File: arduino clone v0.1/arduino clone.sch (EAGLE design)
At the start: 19 parts, among them J202 FTDI Breakout Header, U101 ATMEGA328P_TQFP, U201 CH340G

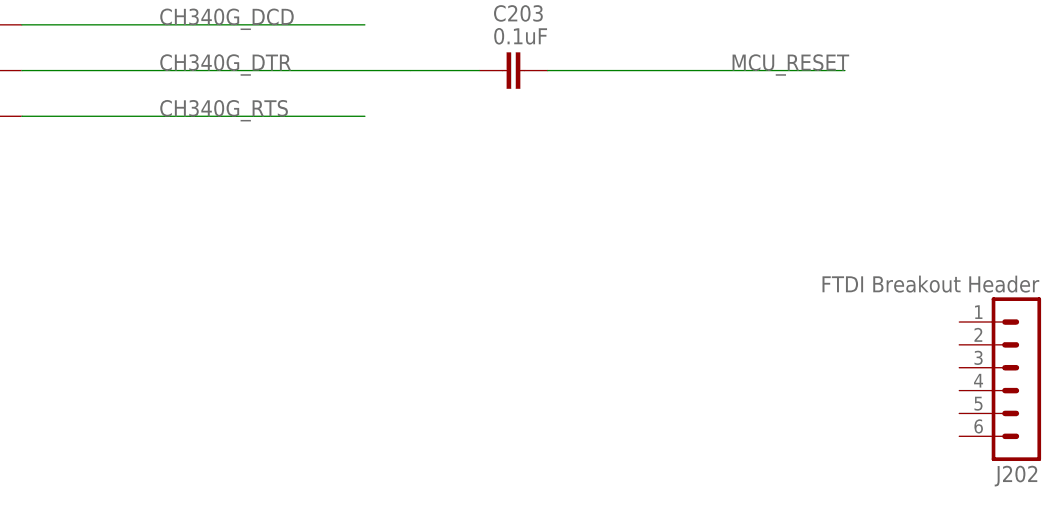
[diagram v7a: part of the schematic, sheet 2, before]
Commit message: add nets from FDTI headers to power and CTS
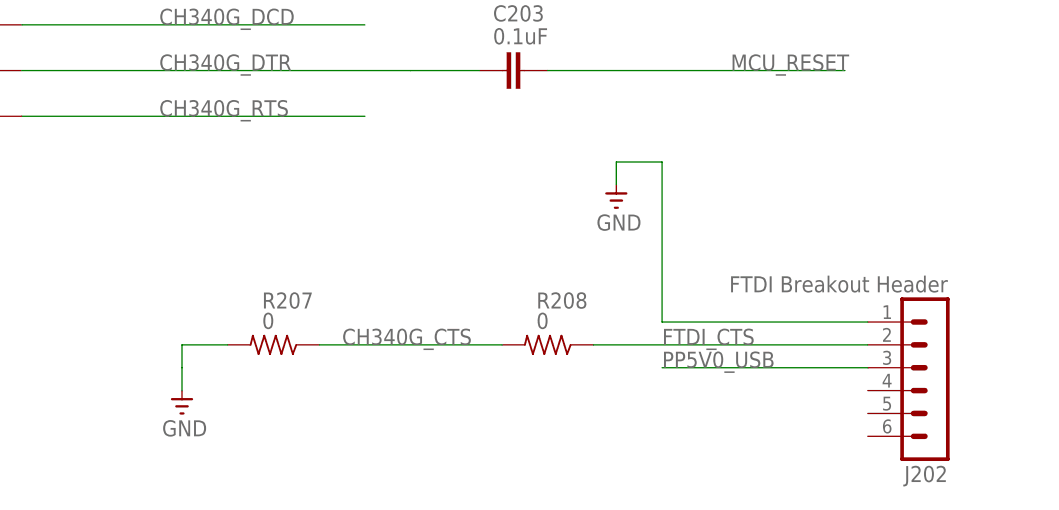
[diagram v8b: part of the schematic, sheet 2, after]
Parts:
- added R207, R208: 0, adafruit:R-US_R0805
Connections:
- new net FTDI_CTS: J202.2, R208.1
- net CH340G_CTS: now also R207.1, R208.2
- net GND: now also J202.1, R207.2
- net PP5V0_USB: now also J202.3
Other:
- moved on the sheet: J202
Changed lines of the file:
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@@
 <part name="C203" library="rcl" library_urn="urn:adsk.eagle:library:334" deviceset="C-EU" device="C0805" package3d_urn="urn:adsk.eagle:package:23617/2" value="0.1uF"/>
 <part name="J202" library="con-lstb" library_urn="urn:adsk.eagle:library:162" deviceset="MA06-1" device="" package3d_urn="urn:adsk.eagle:package:8340/1" value="FTDI Breakout Header"/>
+<part name="GND12" library="supply" deviceset="GND" device=""/>
+<part name="R208" library="adafruit" deviceset="R-US_" device="R0805" value="0"/>
+<part name="R207" library="adafruit" deviceset="R-US_" device="R0805" value="0"/>
+<part name="GND13" library="supply" deviceset="GND" device=""/>
 </parts>
 <sheets>
@@
 <attribute name="VALUE" x="293.624" y="89.281" size="1.778" layer="96"/>
 </instance>
-<instance part="J202" gate="1" x="353.06" y="50.8" rot="R180"/>
+<instance part="J202" gate="1" x="342.9" y="50.8" rot="R180"/>
+<instance part="GND12" gate="1" x="307.34" y="71.12" smashed="yes">
+<attribute name="VALUE" x="305.1175" y="68.58" size="1.778" layer="96"/>
+</instance>
+<instance part="R208" gate="G$1" x="299.72" y="55.88" smashed="yes" rot="R180">
+<attribute name="NAME" x="298.45" y="59.9186" size="1.778" layer="95"/>
+<attribute name="VALUE" x="298.45" y="57.658" size="1.778" layer="96"/>
+</instance>
+<instance part="R207" gate="G$1" x="269.24" y="55.88" smashed="yes" rot="R180">
+<attribute name="NAME" x="267.97" y="59.9186" size="1.778" layer="95"/>
+<attribute name="VALUE" x="267.97" y="57.658" size="1.778" layer="96"/>
+</instance>
+<instance part="GND13" gate="1" x="259.08" y="48.26" smashed="yes">
+<attribute name="VALUE" x="256.8575" y="45.72" size="1.778" layer="96"/>
+</instance>
 </instances>
 <busses>
@@
 <pinref part="R202" gate="G$1" pin="1"/>
 <wire x1="93.98" y1="170.18" x2="93.98" y2="175.26" width="0.1524" layer="91"/>
+</segment>
+<segment>
+<wire x1="307.34" y1="76.2" x2="312.42" y2="76.2" width="0.1524" layer="91"/>
+<wire x1="312.42" y1="76.2" x2="312.42" y2="58.42" width="0.1524" layer="91"/>
+<pinref part="J202" gate="1" pin="1"/>
+<wire x1="312.42" y1="58.42" x2="335.28" y2="58.42" width="0.1524" layer="91"/>
+<pinref part="GND12" gate="1" pin="GND"/>
+<wire x1="307.34" y1="73.66" x2="307.34" y2="76.2" width="0.1524" layer="91"/>
+</segment>
+<segment>
+<pinref part="GND13" gate="1" pin="GND"/>
+<wire x1="259.08" y1="50.8" x2="259.08" y2="53.34" width="0.1524" layer="91"/>
+<wire x1="259.08" y1="53.34" x2="259.08" y2="55.88" width="0.1524" layer="91"/>
+<pinref part="R207" gate="G$1" pin="2"/>
+<wire x1="259.08" y1="55.88" x2="264.16" y2="55.88" width="0.1524" layer="91"/>
 </segment>
 </net>
@@
 <label x="33.02" y="116.84" size="1.778" layer="95"/>
 </segment>
+<segment>
+<pinref part="J202" gate="1" pin="3"/>
+<wire x1="335.28" y1="53.34" x2="312.42" y2="53.34" width="0.1524" layer="91"/>
+<label x="312.42" y="53.34" size="1.778" layer="95"/>
+</segment>
 </net>
 <net name="P_CH340G_D+" class="0">
@@
 <label x="256.54" y="106.68" size="1.778" layer="95"/>
 </segment>
+<segment>
+<pinref part="R207" gate="G$1" pin="1"/>
+<pinref part="R208" gate="G$1" pin="2"/>
+<wire x1="274.32" y1="55.88" x2="294.64" y2="55.88" width="0.1524" layer="91"/>
+<label x="276.86" y="55.88" size="1.778" layer="95"/>
+</segment>
 </net>
 <net name="CH340G_DSR" class="0">
@@
 </segment>
 </net>
+<net name="FTDI_CTS" class="0">
+<segment>
+<pinref part="J202" gate="1" pin="2"/>
+<wire x1="335.28" y1="55.88" x2="304.8" y2="55.88" width="0.1524" layer="91"/>
+<pinref part="R208" gate="G$1" pin="1"/>
+<label x="312.42" y="55.88" size="1.778" layer="95"/>
+</segment>
+</net>
